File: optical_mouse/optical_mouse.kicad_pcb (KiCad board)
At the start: 2 copper layers, 48.3 x 45.7 mm, 18 parts, among them U1 NANO

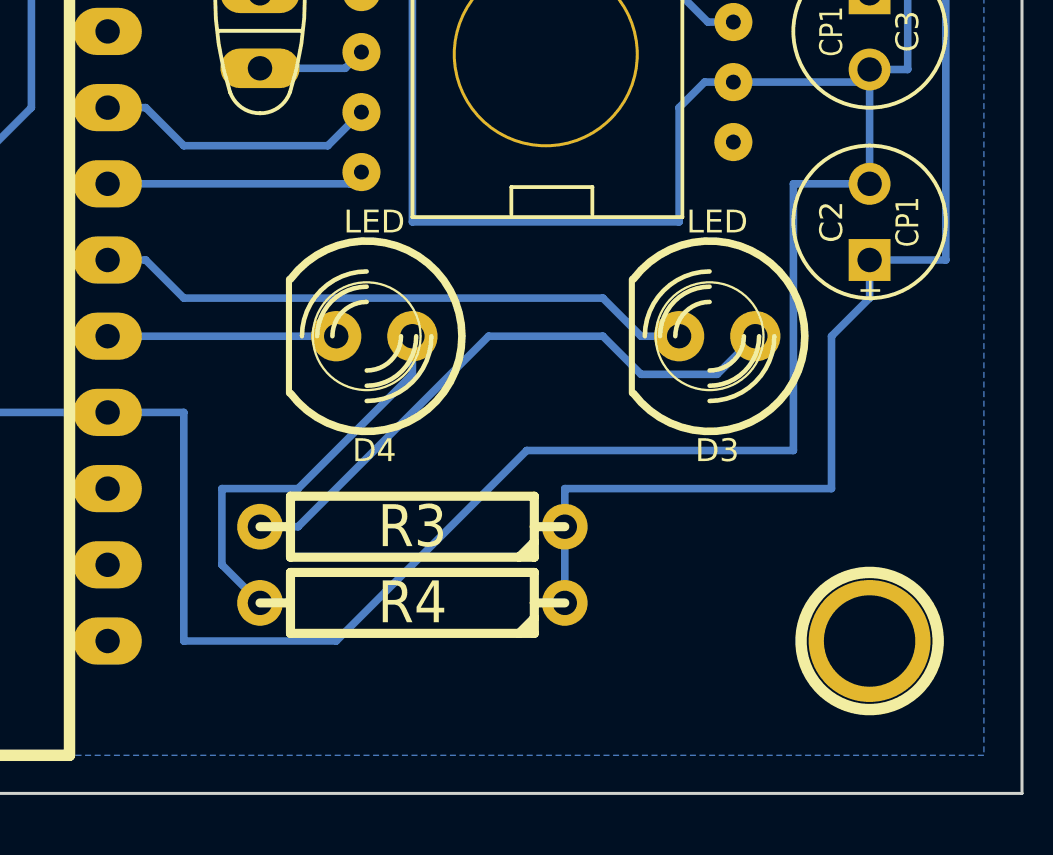
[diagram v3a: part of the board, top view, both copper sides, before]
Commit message: make gnd trace thicker at pinch point
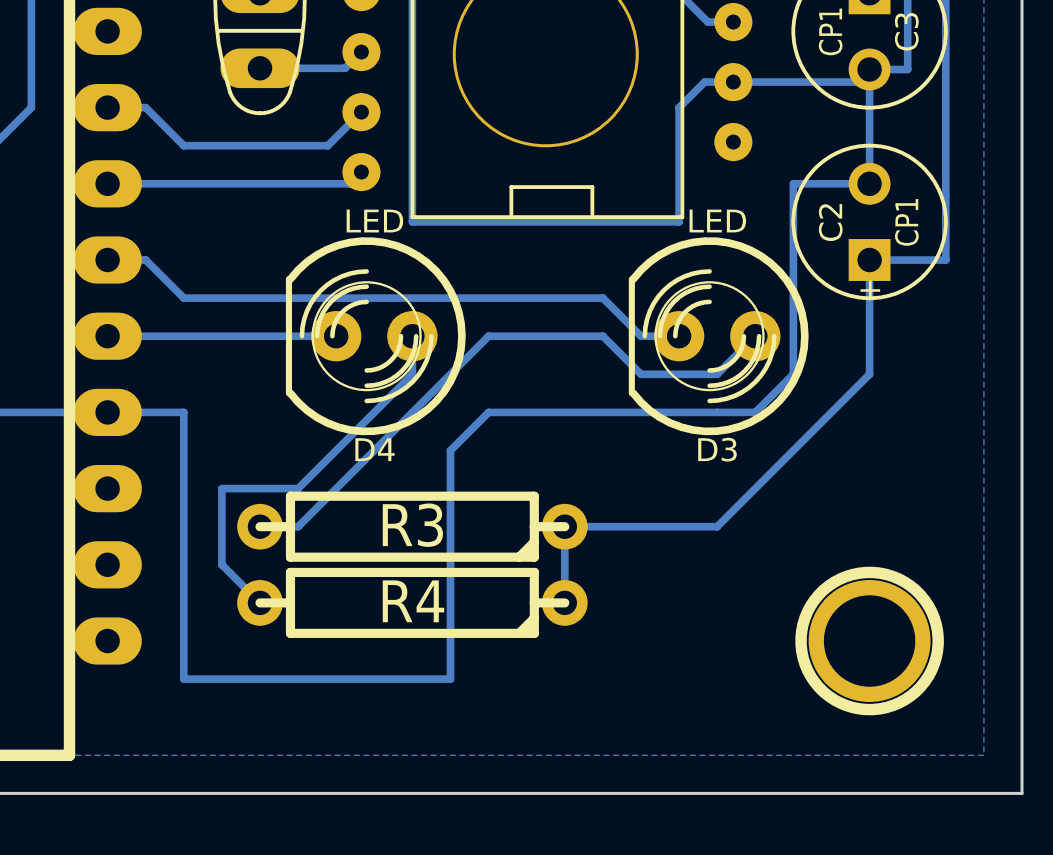
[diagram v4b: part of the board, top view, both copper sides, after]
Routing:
- net GND: track 117.3 -> 122.1 mm
- net +5V: track 131.0 -> 128.7 mm
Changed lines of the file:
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@@
     (thickness 1.6)
     (drawings 4)
-    (tracks 98)
+    (tracks 99)
     (zones 0)
     (modules 18)
@@
   (gr_line (start 193.04 105.41) (end 193.04 151.13) (angle 90) (layer Edge.Cuts) (width 0.1))
   (gr_line (start 144.78 105.41) (end 193.04 105.41) (angle 90) (layer Edge.Cuts) (width 0.1))
+  (segment (start 187.96 137.16) (end 187.96 133.35) (width 0.254) (layer B.Cu) (net 1))
+  (segment (start 182.88 142.24) (end 187.96 137.16) (width 0.254) (layer B.Cu) (net 1))
+  (segment (start 177.8 142.24) (end 182.88 142.24) (width 0.254) (layer B.Cu) (net 1))
   (segment (start 147.32 138.43) (end 149.86 138.43) (width 0.254) (layer B.Cu) (net 1))
   (segment (start 177.8 107.95) (end 177.8 110.49) (width 0.254) (layer B.Cu) (net 1))
@@
   (segment (start 187.96 115.57) (end 187.96 118.11) (width 0.254) (layer B.Cu) (net 1))
   (segment (start 187.96 133.35) (end 190.5 133.35) (width 0.254) (layer B.Cu) (net 1))
+  (segment (start 190.5 133.35) (end 190.5 115.57) (width 0.254) (layer B.Cu) (net 1))
   (segment (start 190.5 115.57) (end 187.96 115.57) (width 0.254) (layer B.Cu) (net 1))
-  (segment (start 190.5 133.35) (end 190.5 115.57) (width 0.254) (layer B.Cu) (net 1))
-  (segment (start 177.8 142.24) (end 177.8 140.97) (width 0.254) (layer B.Cu) (net 1))
-  (segment (start 187.96 134.62) (end 187.96 133.35) (width 0.254) (layer B.Cu) (net 1))
-  (segment (start 186.69 135.89) (end 187.96 134.62) (width 0.254) (layer B.Cu) (net 1))
-  (segment (start 186.69 140.97) (end 186.69 135.89) (width 0.254) (layer B.Cu) (net 1))
-  (segment (start 177.8 140.97) (end 186.69 140.97) (width 0.254) (layer B.Cu) (net 1))
   (segment (start 177.8 113.03) (end 177.8 114.3) (width 0.254) (layer B.Cu) (net 1))
   (segment (start 177.8 114.3) (end 179.07 115.57) (width 0.254) (layer B.Cu) (net 1))
@@
   (segment (start 177.8 113.03) (end 177.8 110.49) (width 0.254) (layer B.Cu) (net 1))
   (segment (start 177.8 144.78) (end 177.8 142.24) (width 0.254) (layer B.Cu) (net 1))
+  (segment (start 185.42 130.81) (end 187.96 130.81) (width 0.254) (layer B.Cu) (net 2))
+  (segment (start 185.42 137.16) (end 185.42 130.81) (width 0.254) (layer B.Cu) (net 2))
+  (segment (start 184.15 138.43) (end 185.42 137.16) (width 0.254) (layer B.Cu) (net 2))
+  (segment (start 182.88 138.43) (end 184.15 138.43) (width 0.254) (layer B.Cu) (net 2))
+  (segment (start 175.26 138.43) (end 182.88 138.43) (width 0.254) (layer B.Cu) (net 2))
+  (segment (start 173.99 139.7) (end 175.26 138.43) (width 0.254) (layer B.Cu) (net 2))
+  (segment (start 173.99 147.32) (end 173.99 139.7) (width 0.254) (layer B.Cu) (net 2))
+  (segment (start 165.1 147.32) (end 173.99 147.32) (width 0.254) (layer B.Cu) (net 2))
+  (segment (start 165.1 138.43) (end 165.1 147.32) (width 0.254) (layer B.Cu) (net 2))
   (segment (start 162.56 138.43) (end 165.1 138.43) (width 0.254) (layer B.Cu) (net 2))
-  (segment (start 185.42 130.81) (end 187.96 130.81) (width 0.254) (layer B.Cu) (net 2))
-  (segment (start 185.42 139.7) (end 185.42 130.81) (width 0.254) (layer B.Cu) (net 2))
-  (segment (start 176.53 139.7) (end 185.42 139.7) (width 0.254) (layer B.Cu) (net 2))
-  (segment (start 170.18 146.05) (end 176.53 139.7) (width 0.254) (layer B.Cu) (net 2))
-  (segment (start 165.1 146.05) (end 170.18 146.05) (width 0.254) (layer B.Cu) (net 2))
-  (segment (start 165.1 138.43) (end 165.1 146.05) (width 0.254) (layer B.Cu) (net 2))
   (segment (start 147.32 143.51) (end 149.86 143.51) (width 0.254) (layer B.Cu) (net 2))
   (segment (start 154.94 138.43) (end 162.56 138.43) (width 0.254) (layer B.Cu) (net 2))
@@
   (segment (start 165.1 120.65) (end 170.18 120.65) (width 0.254) (layer B.Cu) (net 2))
   (segment (start 165.1 124.46) (end 165.1 120.65) (width 0.254) (layer B.Cu) (net 2))
-  (segment (start 172.72 135.89) (end 172.72 137.16) (width 0.254) (layer B.Cu) (net 3) (status 400000))
-  (segment (start 166.37 143.51) (end 167.64 144.78) (width 0.254) (layer B.Cu) (net 3) (status 800000))
+  (segment (start 172.72 135.89) (end 172.72 137.16) (width 0.254) (layer B.Cu) (net 3))
+  (segment (start 166.37 143.51) (end 167.64 144.78) (width 0.254) (layer B.Cu) (net 3))
   (segment (start 166.37 140.97) (end 166.37 143.51) (width 0.254) (layer B.Cu) (net 3))
   (segment (start 168.91 140.97) (end 166.37 140.97) (width 0.254) (layer B.Cu) (net 3))
   (segment (start 172.72 137.16) (end 168.91 140.97) (width 0.254) (layer B.Cu) (net 3))
-  (segment (start 162.56 133.35) (end 163.83 133.35) (width 0.254) (layer B.Cu) (net 4) (status 400000))
-  (segment (start 180.34 135.89) (end 181.61 135.89) (width 0.254) (layer B.Cu) (net 4) (status 800000))
+  (segment (start 162.56 133.35) (end 163.83 133.35) (width 0.254) (layer B.Cu) (net 4))
+  (segment (start 180.34 135.89) (end 181.61 135.89) (width 0.254) (layer B.Cu) (net 4))
   (segment (start 179.07 134.62) (end 180.34 135.89) (width 0.254) (layer B.Cu) (net 4))
   (segment (start 165.1 134.62) (end 179.07 134.62) (width 0.254) (layer B.Cu) (net 4))
@@
   (segment (start 166.37 109.22) (end 168.91 109.22) (width 0.254) (layer B.Cu) (net 6))
   (segment (start 165.1 110.49) (end 166.37 109.22) (width 0.254) (layer B.Cu) (net 6))
-  (segment (start 162.56 130.81) (end 170.62958 130.81) (width 0.254) (layer B.Cu) (net 7) (status C00000))
-  (segment (start 170.62958 130.81) (end 171.02074 130.41884) (width 0.254) (layer B.Cu) (net 7) (status C00000))
-  (segment (start 162.56 128.27) (end 163.83 128.27) (width 0.254) (layer B.Cu) (net 8) (status 400000))
-  (segment (start 169.9006 129.54) (end 171.02074 128.41986) (width 0.254) (layer B.Cu) (net 8) (status 800000))
+  (segment (start 162.56 130.81) (end 170.62958 130.81) (width 0.254) (layer B.Cu) (net 7))
+  (segment (start 170.62958 130.81) (end 171.02074 130.41884) (width 0.254) (layer B.Cu) (net 7))
+  (segment (start 162.56 128.27) (end 163.83 128.27) (width 0.254) (layer B.Cu) (net 8))
+  (segment (start 169.9006 129.54) (end 171.02074 128.41986) (width 0.254) (layer B.Cu) (net 8))
   (segment (start 165.1 129.54) (end 169.9006 129.54) (width 0.254) (layer B.Cu) (net 8))
   (segment (start 163.83 128.27) (end 165.1 129.54) (width 0.254) (layer B.Cu) (net 8))
@@
   (segment (start 185.42 124.46) (end 187.96 124.46) (width 0.254) (layer B.Cu) (net 11))
   (segment (start 184.3786 123.4186) (end 185.42 124.46) (width 0.254) (layer B.Cu) (net 11))
-  (segment (start 162.56 113.03) (end 165.1 113.03) (width 0.254) (layer B.Cu) (net 12) (status 400000))
-  (segment (start 170.18 116.84) (end 170.18 118.11) (width 0.254) (layer B.Cu) (net 12) (status 800000))
+  (segment (start 162.56 113.03) (end 165.1 113.03) (width 0.254) (layer B.Cu) (net 12))
+  (segment (start 170.18 116.84) (end 170.18 118.11) (width 0.254) (layer B.Cu) (net 12))
   (segment (start 165.1 116.84) (end 170.18 116.84) (width 0.254) (layer B.Cu) (net 12))
   (segment (start 165.1 113.03) (end 165.1 116.84) (width 0.254) (layer B.Cu) (net 12))

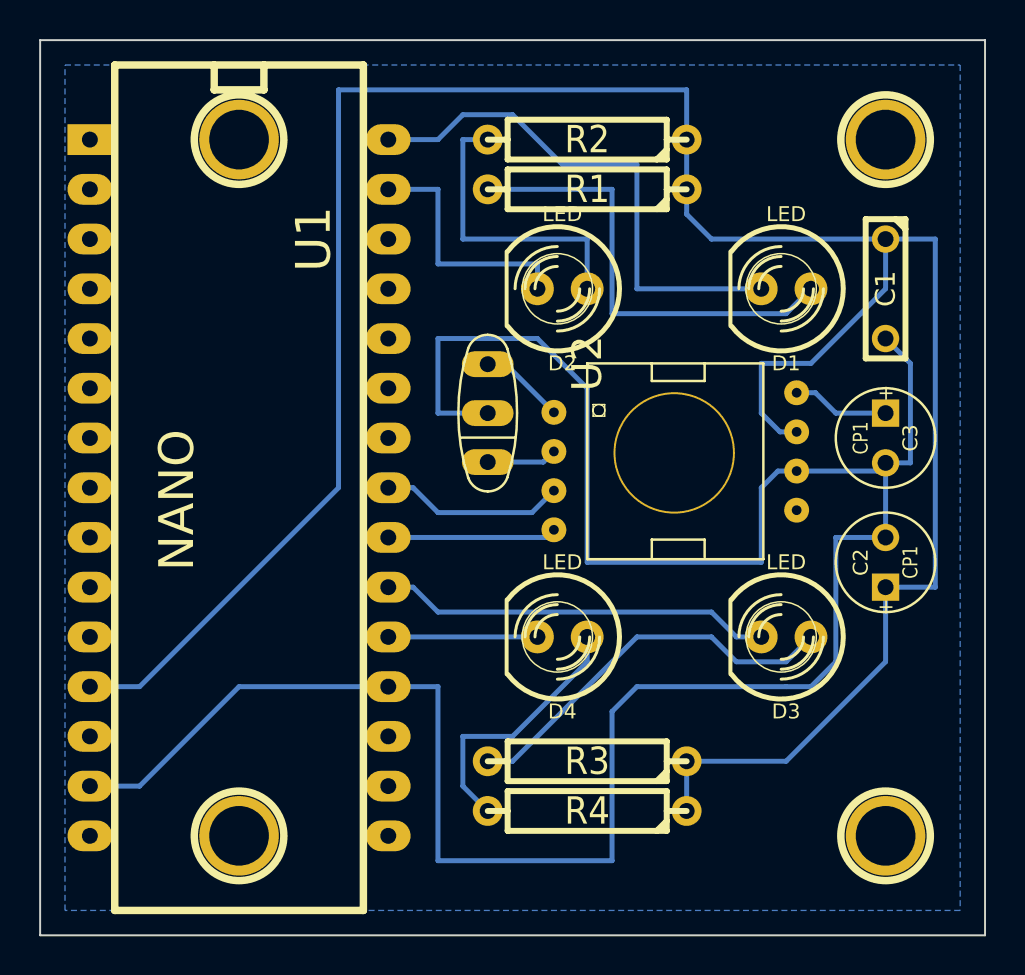
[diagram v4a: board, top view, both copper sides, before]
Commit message: arrange LEDs around circle
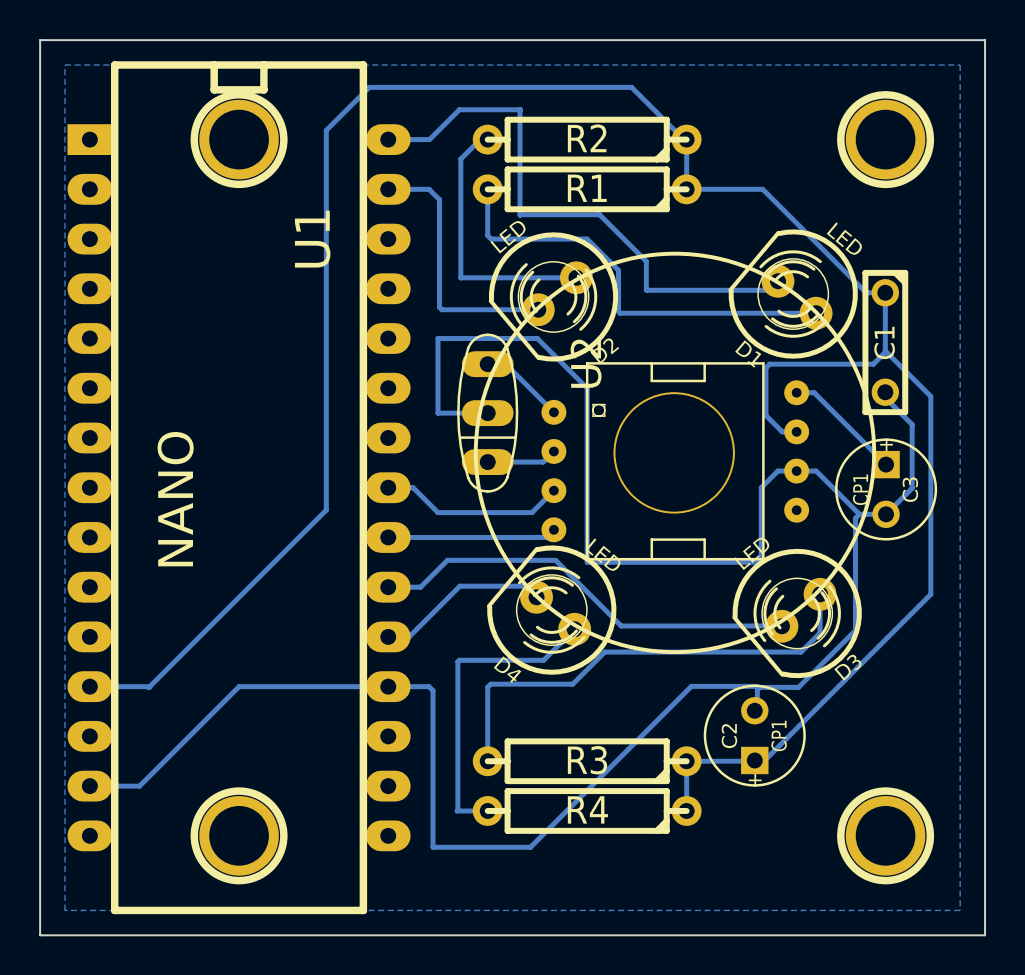
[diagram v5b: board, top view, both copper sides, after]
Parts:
- moved C2 11.1 mm to (181.3, 140.9)
- moved C1 2.74 mm to (187.9, 120.9)
- moved C3 2.63 mm to (188.0, 128.4)
- moved D3 1.56 mm to (183.6, 134.5), turned to 220 degrees
- moved D4 1.25 mm to (171.1, 134.7), turned to 140 degrees
- moved D1 0.71 mm to (183.4, 118.5), turned to 140 degrees
- moved D2 0.36 mm to (171.2, 118.4), turned to 220 degrees
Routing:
- net +5V: track 128.7 -> 116.4 mm
- net GND: track 122.1 -> 112.9 mm
- net N-000009: track 20.2 -> 23.9 mm
- net N-000001: track 13.5 -> 15.8 mm
- net N-0000011: track 20.1 -> 22.1 mm
- net N-0000019: track 27.0 -> 28.6 mm
- net N-000008: track 15.2 -> 13.8 mm
- net N-000007: track 23.4 -> 22.0 mm
- net N-0000018: track 7.62 -> 8.88 mm
- net N-0000034: track 4.97 -> 6.09 mm
- net N-000006: track 12.7 -> 13.4 mm

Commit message: minor moves
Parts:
- moved R3 2.54 mm to (172.7, 144.8)
- moved R4 2.54 mm to (172.7, 142.2)
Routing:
- net N-000001: track 15.8 -> 9.46 mm
- net N-000009: track 23.9 -> 25.3 mm
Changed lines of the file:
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@@
     (thickness 1.6)
     (drawings 5)
-    (tracks 125)
+    (tracks 124)
     (zones 0)
     (modules 18)
@@
   )
   (module R4 (layer F.Cu)
-    (at 172.72 142.24 180)
+    (at 172.72 144.78 180)
     (descr "Resitance 4 pas")
     (tags R)
@@
   )
   (module R4 (layer F.Cu)
-    (at 172.72 144.78 180)
+    (at 172.72 142.24 180)
     (descr "Resitance 4 pas")
     (tags R)
@@
   (gr_line (start 193.04 105.41) (end 193.04 151.13) (angle 90) (layer Edge.Cuts) (width 0.1))
   (gr_line (start 144.78 105.41) (end 193.04 105.41) (angle 90) (layer Edge.Cuts) (width 0.1))
+  (segment (start 177.8 142.24) (end 181.2417 142.24) (width 0.254) (layer B.Cu) (net 1))
+  (segment (start 181.2417 142.24) (end 181.2798 142.2019) (width 0.254) (layer B.Cu) (net 1))
+  (segment (start 177.8 144.78) (end 177.8 142.24) (width 0.254) (layer B.Cu) (net 1))
   (segment (start 181.2798 142.2019) (end 181.7878 142.2019) (width 0.254) (layer B.Cu) (net 1))
+  (segment (start 181.7878 142.2019) (end 190.2714 133.7183) (width 0.254) (layer B.Cu) (net 1))
+  (segment (start 190.2714 133.7183) (end 190.2714 123.6091) (width 0.254) (layer B.Cu) (net 1))
   (segment (start 190.2714 123.6091) (end 187.9473 121.285) (width 0.254) (layer B.Cu) (net 1))
-  (segment (start 190.2714 133.7183) (end 190.2714 123.6091) (width 0.254) (layer B.Cu) (net 1))
-  (segment (start 181.7878 142.2019) (end 190.2714 133.7183) (width 0.254) (layer B.Cu) (net 1))
   (segment (start 177.8 113.03) (end 181.6862 113.03) (width 0.254) (layer B.Cu) (net 1))
   (segment (start 186.9694 118.3132) (end 187.9473 118.3132) (width 0.254) (layer B.Cu) (net 1))
@@
   (segment (start 187.3377 121.9581) (end 182.0418 121.9581) (width 0.254) (layer B.Cu) (net 1))
   (segment (start 187.9473 121.3485) (end 187.3377 121.9581) (width 0.254) (layer B.Cu) (net 1))
-  (segment (start 177.8 142.24) (end 181.2417 142.24) (width 0.254) (layer B.Cu) (net 1))
-  (segment (start 181.2417 142.24) (end 181.2798 142.2019) (width 0.254) (layer B.Cu) (net 1))
   (segment (start 147.32 138.43) (end 150.3807 138.43) (width 0.254) (layer B.Cu) (net 1))
   (segment (start 177.6603 110.49) (end 174.9933 107.823) (width 0.254) (layer B.Cu) (net 1))
@@
   (segment (start 150.3807 138.43) (end 150.3299 138.4808) (width 0.254) (layer B.Cu) (net 1))
   (segment (start 177.8 113.03) (end 177.8 110.49) (width 0.254) (layer B.Cu) (net 1))
-  (segment (start 177.8 144.78) (end 177.8 142.24) (width 0.254) (layer B.Cu) (net 1))
   (segment (start 187.9473 123.3932) (end 187.9473 123.6726) (width 0.254) (layer B.Cu) (net 2))
   (segment (start 189.3189 128.2954) (end 187.9854 129.6289) (width 0.254) (layer B.Cu) (net 2))
@@
   (segment (start 165.1 120.65) (end 170.18 120.65) (width 0.254) (layer B.Cu) (net 2))
   (segment (start 165.1 124.46) (end 165.1 120.65) (width 0.254) (layer B.Cu) (net 2))
-  (segment (start 167.64 144.78) (end 166.0779 144.78) (width 0.254) (layer B.Cu) (net 3))
-  (segment (start 170.496016 137.0838) (end 172.079976 135.49984) (width 0.254) (layer B.Cu) (net 3))
-  (segment (start 166.1922 137.0838) (end 170.496016 137.0838) (width 0.254) (layer B.Cu) (net 3))
-  (segment (start 166.116 137.16) (end 166.1922 137.0838) (width 0.254) (layer B.Cu) (net 3))
-  (segment (start 166.116 144.7419) (end 166.116 137.16) (width 0.254) (layer B.Cu) (net 3))
-  (segment (start 166.0779 144.78) (end 166.116 144.7419) (width 0.254) (layer B.Cu) (net 3))
+  (segment (start 167.64 142.24) (end 167.64 138.43) (width 0.254) (layer B.Cu) (net 3))
+  (segment (start 170.419816 137.16) (end 172.079976 135.49984) (width 0.254) (layer B.Cu) (net 3))
+  (segment (start 168.91 137.16) (end 170.419816 137.16) (width 0.254) (layer B.Cu) (net 3))
+  (segment (start 167.64 138.43) (end 168.91 137.16) (width 0.254) (layer B.Cu) (net 3))
   (segment (start 162.56 133.35) (end 164.211 133.35) (width 0.254) (layer B.Cu) (net 4))
   (segment (start 182.652884 135.3312) (end 182.669124 135.34744) (width 0.254) (layer B.Cu) (net 4))
@@
   (segment (start 166.2684 111.4806) (end 166.2684 117.5512) (width 0.254) (layer B.Cu) (net 14))
   (segment (start 167.259 110.49) (end 166.2684 111.4806) (width 0.254) (layer B.Cu) (net 14))
-  (segment (start 167.64 142.24) (end 167.64 138.4554) (width 0.254) (layer B.Cu) (net 15))
-  (segment (start 184.614876 135.691824) (end 184.614876 133.71476) (width 0.254) (layer B.Cu) (net 15))
-  (segment (start 183.642 136.6647) (end 184.614876 135.691824) (width 0.254) (layer B.Cu) (net 15))
-  (segment (start 173.6217 136.6647) (end 183.642 136.6647) (width 0.254) (layer B.Cu) (net 15))
-  (segment (start 171.9834 138.303) (end 173.6217 136.6647) (width 0.254) (layer B.Cu) (net 15))
-  (segment (start 167.7924 138.303) (end 171.9834 138.303) (width 0.254) (layer B.Cu) (net 15))
-  (segment (start 167.64 138.4554) (end 167.7924 138.303) (width 0.254) (layer B.Cu) (net 15))
+  (segment (start 184.614876 133.71476) (end 184.614876 135.719876) (width 0.254) (layer B.Cu) (net 15))
+  (segment (start 168.91 143.51) (end 167.64 144.78) (width 0.254) (layer B.Cu) (net 15))
+  (segment (start 168.91 139.065) (end 168.91 143.51) (width 0.254) (layer B.Cu) (net 15))
+  (segment (start 169.545 138.43) (end 168.91 139.065) (width 0.254) (layer B.Cu) (net 15))
+  (segment (start 170.815 138.43) (end 169.545 138.43) (width 0.254) (layer B.Cu) (net 15))
+  (segment (start 172.425248 136.819752) (end 170.815 138.43) (width 0.254) (layer B.Cu) (net 15))
+  (segment (start 183.515 136.819752) (end 172.425248 136.819752) (width 0.254) (layer B.Cu) (net 15))
+  (segment (start 184.614876 135.719876) (end 183.515 136.819752) (width 0.254) (layer B.Cu) (net 15))
   (zone (net 0) (net_name "") (layer B.Cu) (hatch edge 0.508)
     (connect_pads (clearance 0.508))
